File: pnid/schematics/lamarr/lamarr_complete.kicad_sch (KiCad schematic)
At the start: 68 parts

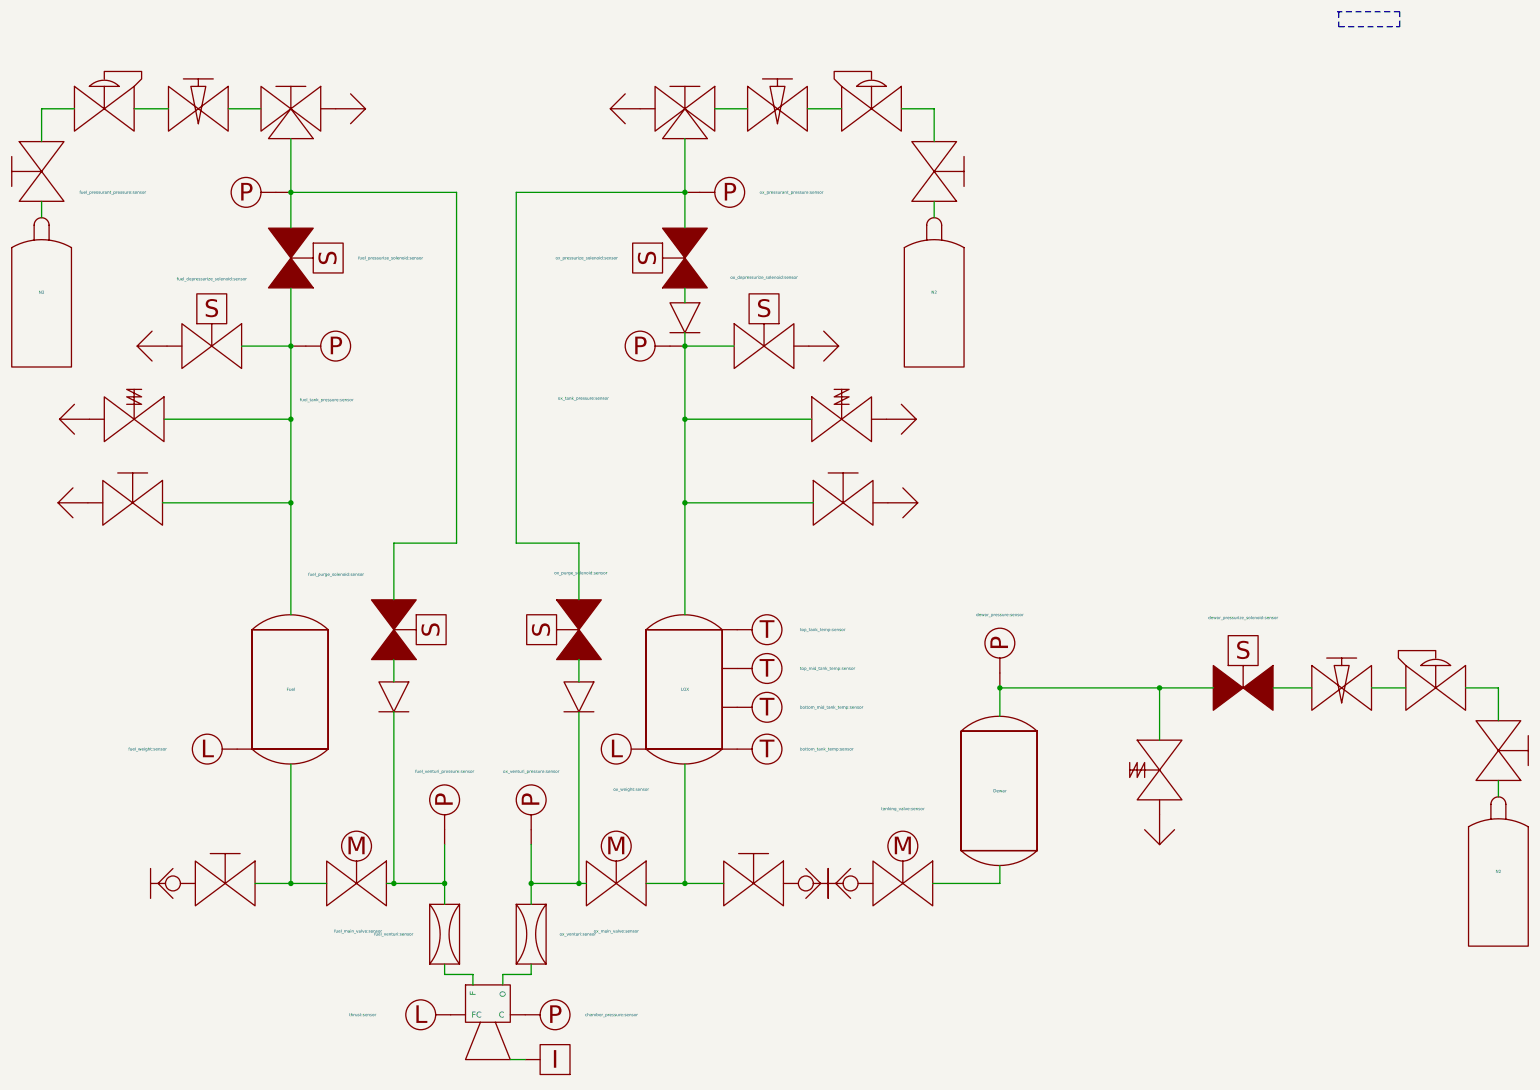
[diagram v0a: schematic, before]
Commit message: update to kicad 8 and fix migration issues
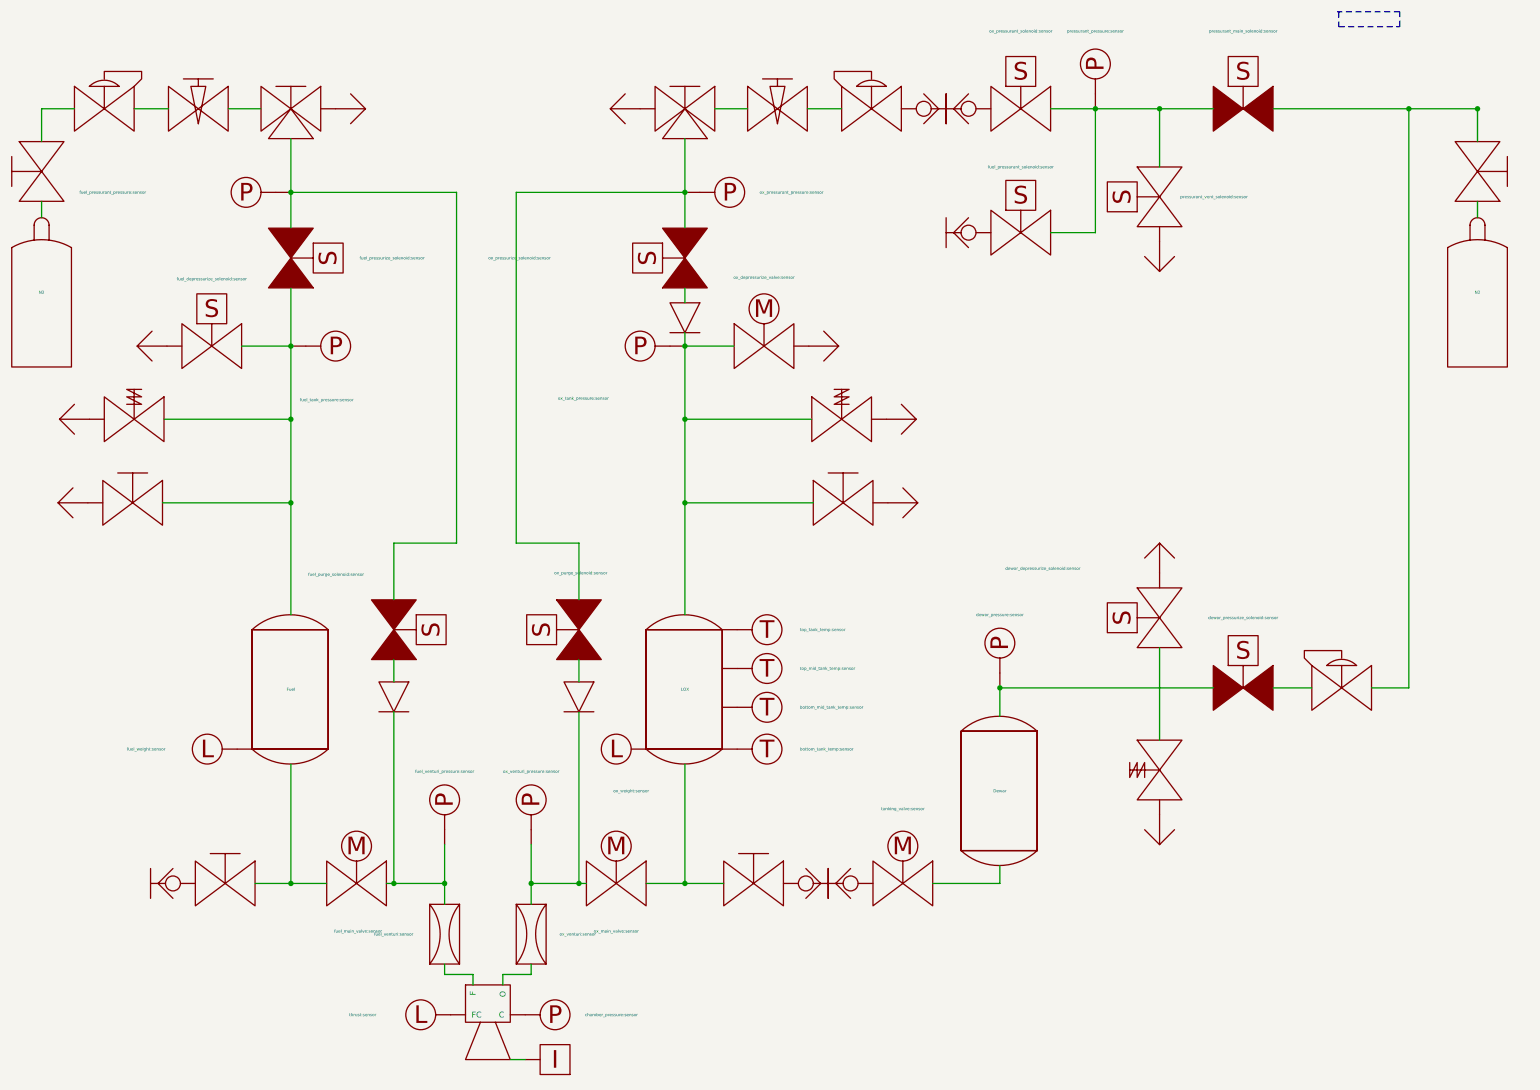
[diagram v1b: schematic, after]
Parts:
- removed N2 (x2): N2, symbol lamarr-rescue:GasBottle-PnID-Lib
- removed Vent?: Vent, symbol lamarr-rescue:Vent-PnID-Lib
- removed dewar_manual_valve?: dewar_manual_valve, symbol lamarr-rescue:Valve_Manual-PnID-Lib
- removed dewar_needle_valve?: dewar_needle_valve, symbol lamarr-rescue:Valve_Needle-PnID-Lib
- removed dewar_pressure_regulator?: dewar_pressure_regulator, symbol lamarr-rescue:PressureRegulator-PnID-Lib
- removed fuel_weight: fuel_weight:sensor, symbol lamarr-rescue:Sensor_Load-PnID-Lib
- removed ox_manual_valve?: ox_manual_valve, symbol lamarr-rescue:Valve_Manual-PnID-Lib
- removed ox_weight: ox_weight:sensor, symbol lamarr-rescue:Sensor_Load_Short-PnID-Lib
- added DewarPressureRegulator?: DewarPressureRegulator, symbol lamarr_complete-rescue:PressureRegulator-PnID-Lib
- added N2: N2, symbol lamarr_complete-rescue:GasBottle-PnID-Lib
- added QuickConnect?: QuickConnect_Half, symbol lamarr_complete-rescue:QuickConnect_Half-PnID-Lib
- added Vent? (x3): Vent, symbol lamarr_complete-rescue:Vent-PnID-Lib
- added dewar_depressurize_solenoid?: dewar_depressurize_solenoid:sensor, symbol lamarr_complete-rescue:Valve_Solenoid_NO-PnID-Lib
- added fuel_pressurant_solenoid?: fuel_pressurant_solenoid:sensor, symbol lamarr_complete-rescue:Valve_Solenoid_NO-PnID-Lib
- added fuel_quick_connect?: fuel_quick_connect, symbol lamarr_complete-rescue:QuickConnect_Half-PnID-Lib
- added fuel_weight: fuel_weight:sensor, symbol lamarr_complete-rescue:Sensor_Load-PnID-Lib
- added ox_manual_valve: ox_manual_valve, symbol lamarr_complete-rescue:Valve_Manual-PnID-Lib
- added ox_pressurant_solenoid?: ox_pressurant_solenoid:sensor, symbol lamarr_complete-rescue:Valve_Solenoid_NO-PnID-Lib
- added ox_quick_connect?: ox_quick_connect, symbol lamarr_complete-rescue:QuickConnect_Half-PnID-Lib
- added ox_weight: ox_weight:sensor, symbol lamarr_complete-rescue:Sensor_Load_Short-PnID-Lib
- added pressurant_main_solenoid?: pressurant_main_solenoid:sensor, symbol lamarr_complete-rescue:Valve_Solenoid_NC-PnID-Lib
- added pressurant_pressure?: pressurant_pressure:sensor, symbol lamarr_complete-rescue:Sensor_Pressure-PnID-Lib
- added pressurant_vent_solenoid?: pressurant_vent_solenoid:sensor, symbol lamarr_complete-rescue:Valve_Solenoid_NO-PnID-Lib
- CheckValve? (x3): symbol lamarr-rescue:CheckValve-PnID-Lib -> lamarr_complete-rescue:CheckValve-PnID-Lib
- Dewar, Fuel, LOX: symbol lamarr-rescue:Tank_Slim-PnID-Lib -> lamarr_complete-rescue:Tank_Slim-PnID-Lib
- DewarOverPressureValve?, fuel_safety_valve, ox_safety_valve: symbol lamarr-rescue:Valve_OverPressure-PnID-Lib -> lamarr_complete-rescue:Valve_OverPressure-PnID-Lib
- DewarQuickConnect?, fuel_quick_connect, ox_quick_connect: symbol lamarr-rescue:QuickConnect_Half-PnID-Lib -> lamarr_complete-rescue:QuickConnect_Half-PnID-Lib
- N2: symbol lamarr-rescue:GasBottle-PnID-Lib -> lamarr_complete-rescue:GasBottle-PnID-Lib
- Vent? (x8): symbol lamarr-rescue:Vent-PnID-Lib -> lamarr_complete-rescue:Vent-PnID-Lib
- bottom_mid_tank_temp, bottom_tank_temp, top_mid_tank_temp, top_tank_temp: symbol lamarr-rescue:Sensor_Temperature-PnID-Lib -> lamarr_complete-rescue:Sensor_Temperature-PnID-Lib
- chamber_pressure, dewar_pressure?, fuel_pressurant_pressure, fuel_tank_pressure, fuel_venturi_pressure, ox_pressurant_pressure:sensor, ox_tank_pressure, ox_venturi_pressure: symbol lamarr-rescue:Sensor_Pressure-PnID-Lib -> lamarr_complete-rescue:Sensor_Pressure-PnID-Lib
- dewar_pressurize_solenoid?, fuel_pressurize_solenoid, fuel_purge_solenoid, ox_pressurize_solenoid, ox_purge_solenoid: symbol lamarr-rescue:Valve_Solenoid_NC-PnID-Lib -> lamarr_complete-rescue:Valve_Solenoid_NC-PnID-Lib
- engine: symbol lamarr-rescue:Engine-PnID-Lib -> lamarr_complete-rescue:Engine-PnID-Lib
- fuel_depressurize_solenoid: symbol lamarr-rescue:Valve_Solenoid_NO-PnID-Lib -> lamarr_complete-rescue:Valve_Solenoid_NO-PnID-Lib
- fuel_main_valve, ox_main_valve, tanking_valve?: symbol lamarr-rescue:Valve_Servo-PnID-Lib -> lamarr_complete-rescue:Valve_Servo-PnID-Lib
- fuel_manual_3way, fuel_manual_3way?: symbol lamarr-rescue:Valve_Manual_3Way-PnID-Lib -> lamarr_complete-rescue:Valve_Manual_3Way-PnID-Lib
- fuel_manual_tanking_valve, fuel_manual_valve, fuel_manual_vent_valve, ox_manual_tanking_valve, ox_manual_vent_valve: symbol lamarr-rescue:Valve_Manual-PnID-Lib -> lamarr_complete-rescue:Valve_Manual-PnID-Lib
- fuel_needle_valve, ox_needle_valve: symbol lamarr-rescue:Valve_Needle-PnID-Lib -> lamarr_complete-rescue:Valve_Needle-PnID-Lib
- fuel_pressure_regulator, ox_pressure_regulator: symbol lamarr-rescue:PressureRegulator-PnID-Lib -> lamarr_complete-rescue:PressureRegulator-PnID-Lib
- fuel_venturi, ox_venturi: symbol lamarr-rescue:Venturi-PnID-Lib -> lamarr_complete-rescue:Venturi-PnID-Lib
- igniter: symbol lamarr-rescue:igniter-PnID-Lib -> lamarr_complete-rescue:igniter-PnID-Lib
- ox_depressurize_valve: renamed from ox_depressurize_solenoid; value ox_depressurize_solenoid:sensor -> ox_depressurize_valve:sensor; symbol lamarr-rescue:Valve_Solenoid_NO-PnID-Lib -> lamarr_complete-rescue:Valve_Servo-PnID-Lib
- thrust: symbol lamarr-rescue:Sensor_Load-PnID-Lib -> lamarr_complete-rescue:Sensor_Load-PnID-Lib
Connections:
- net at engine.~ (O): now also thrust.~; no longer ox_venturi.~
- net at fuel_venturi.~: now also CheckValve?.~, fuel_main_valve.~, fuel_venturi_pressure.~; no longer engine.~ (O)
- net at Dewar.~, dewar_pressure?.~, dewar_pressurize_solenoid?.~: no longer DewarOverPressureValve?.~
- net at ox_manual_vent_valve.~: now also Vent?.~
- new net: fuel_manual_3way?.~, ox_pressurant_pressure:sensor.~, ox_pressurize_solenoid.~, ox_purge_solenoid.~
- new net: fuel_manual_3way.~, fuel_pressurant_pressure.~, fuel_pressurize_solenoid.~, fuel_purge_solenoid.~
- new net: Fuel.~, fuel_depressurize_solenoid.~, fuel_manual_vent_valve.~, fuel_pressurize_solenoid.~, fuel_safety_valve.~, fuel_tank_pressure.~
- new net: CheckValve?.~, LOX.~, ox_depressurize_valve.~, ox_manual_vent_valve.~, ox_safety_valve.~, ox_tank_pressure.~
- new net: LOX.~, ox_main_valve.~, ox_manual_tanking_valve.~
- new net: Fuel.~, fuel_main_valve.~, fuel_manual_tanking_valve.~
- new net: engine.~ (O), ox_venturi.~
- new net: engine.~ (O), fuel_venturi.~
- new net: DewarPressureRegulator?.~, dewar_pressurize_solenoid?.~
- new net: DewarPressureRegulator?.~, ox_manual_valve.~, pressurant_main_solenoid?.~
- new net: DewarOverPressureValve?.~, dewar_depressurize_solenoid?.~
- new net: fuel_pressurant_solenoid?.~, ox_pressurant_solenoid?.~, pressurant_main_solenoid?.~, pressurant_pressure?.~, pressurant_vent_solenoid?.~
- new net: Vent?.~, pressurant_vent_solenoid?.~
- new net: fuel_pressurant_solenoid?.~, fuel_quick_connect?.~
- new net: ox_pressurant_solenoid?.~, ox_quick_connect?.~
- new net: Vent?.~, dewar_depressurize_solenoid?.~
- new net: N2.~, ox_manual_valve.~
- new net: QuickConnect?.~, ox_pressure_regulator.~
